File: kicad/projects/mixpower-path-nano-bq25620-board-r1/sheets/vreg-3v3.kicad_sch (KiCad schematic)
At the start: 14 parts, among them U13 TPS63802

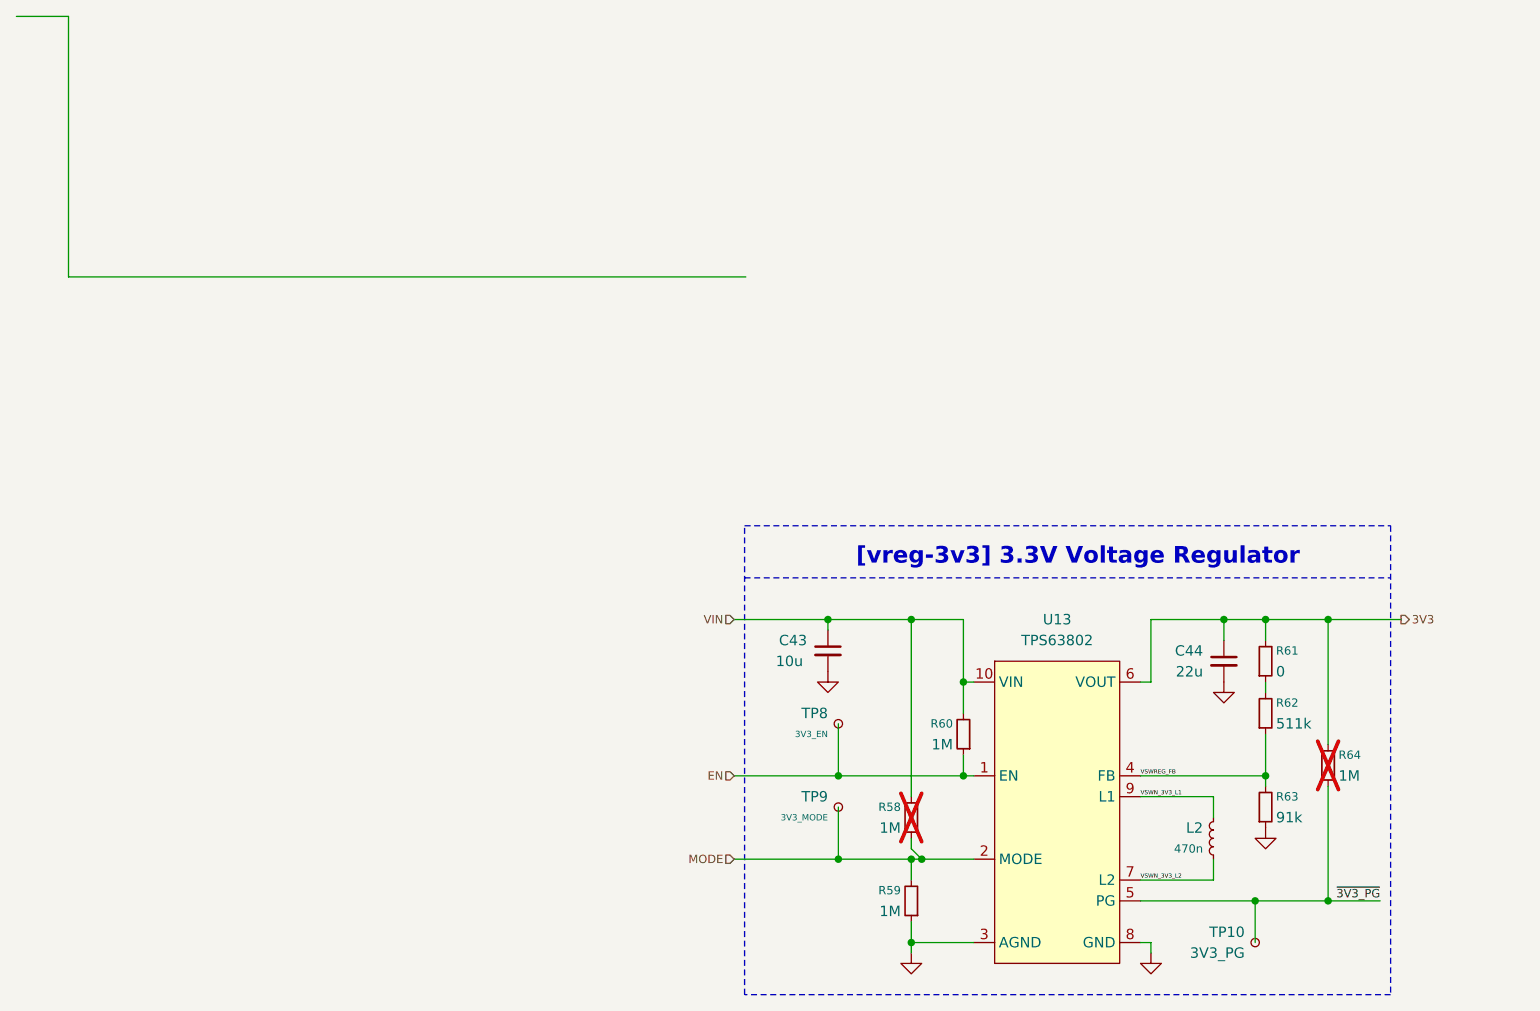
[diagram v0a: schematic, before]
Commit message: feat: rework schematics and add proper calculations
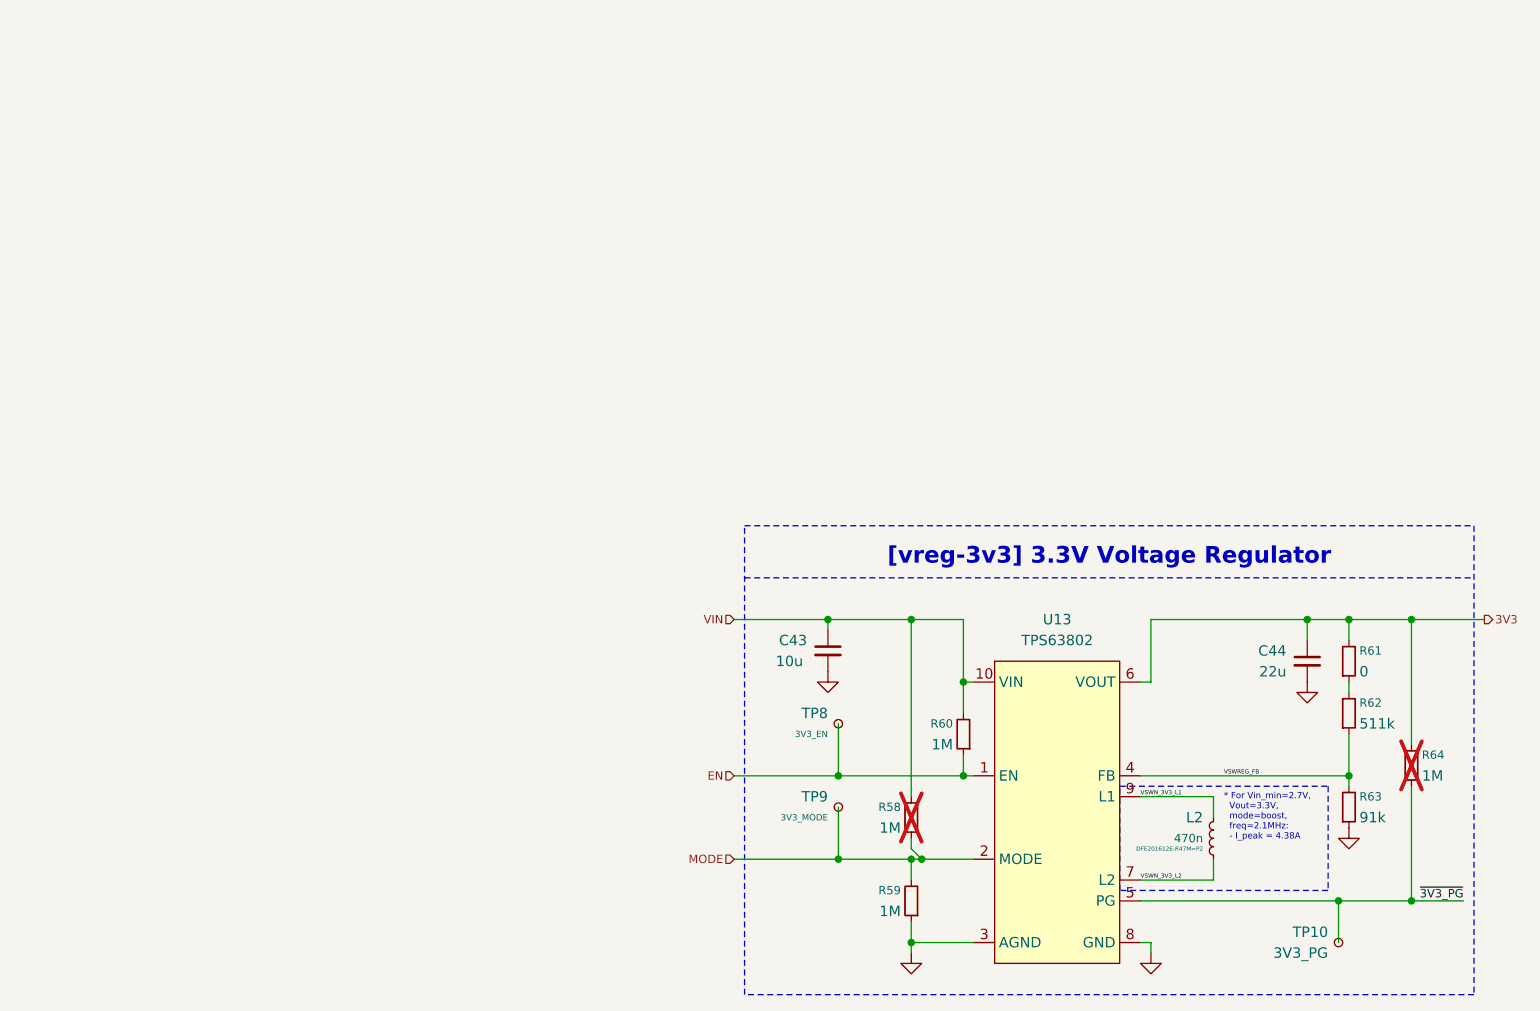
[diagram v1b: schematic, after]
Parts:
- L2: SKU (none) -> DFE201612E-R47M=P2
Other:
- note added: "* For Vin_min=2.7V, Vout=3.3V, mode=boost, freq=2.1MHz: - I_peak = 4.38A"
- moved on the sheet: C44, R61, R62, R63, R64, TP10
